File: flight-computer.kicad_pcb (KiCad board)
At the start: 2 copper layers, 50 x 62 mm, 49 parts, among them J1 Throttle/BEC, J2 Servo 1, J3 Servo 2, J4 Servo 3, J5 Servo 4, J6 Breakout1, J7 Power, J8 Ext, J9 Breakout2, SW1 SW_Push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

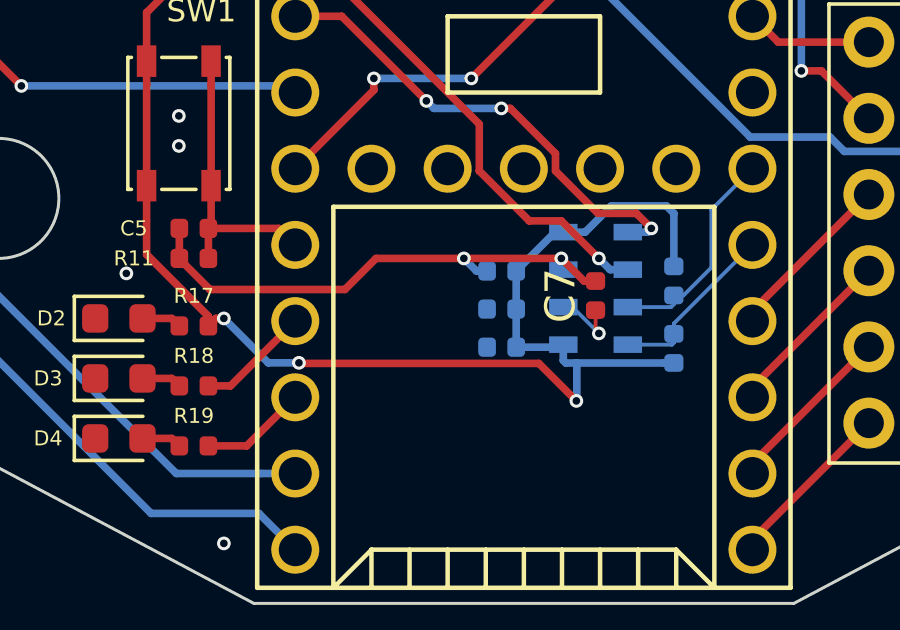
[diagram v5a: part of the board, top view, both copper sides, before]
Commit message: Fixed C4 footprint
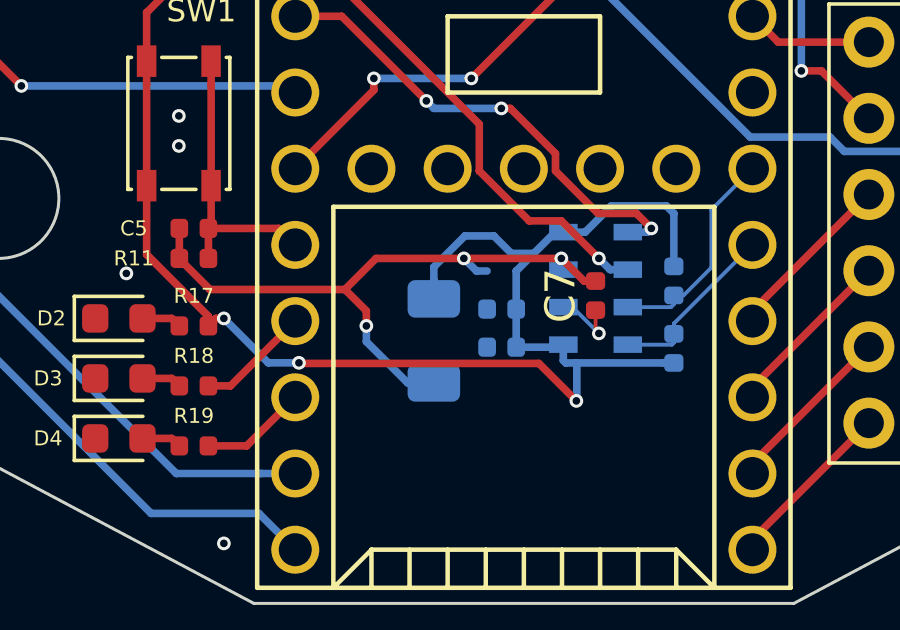
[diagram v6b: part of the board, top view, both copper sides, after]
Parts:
- C4: footprint Capacitor_SMD:C_0402_1005Metric -> Capacitor_SMD:C_1206_3216Metric
- moved C4 3.25 mm to (106.0, 103.2), turned to 270 degrees
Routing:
- net +3V3: track 133.9 -> 138.9 mm
- net GND: track 39.9 -> 44.8 mm, vias 22 -> 23
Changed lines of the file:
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@@
     (thickness 1.6)
     (drawings 12)
-    (tracks 431)
+    (tracks 444)
     (zones 0)
     (modules 49)
@@
     )
   )
-  (module Capacitor_SMD:C_0402_1005Metric (layer B.Cu)
-    (at 108.26 100.92 180)
-    (descr "Capacitor SMD 0402 (1005 Metric), square (rectangular) end terminal, IPC_7351 nominal, (Body size source: http://www.tortai-tech.com/upload/download/2011102023233369053.pdf), generated with kicad-footprint-generator")
-    (tags capacitor)
-    (attr smd)
-    (fp_text reference C4 (at 0 1.17) (layer B.SilkS)
-      (effects (font (size 1 1) (thickness 0.15)) (justify mirror))
-    )
-    (fp_text value 10uF (at 0 -1.17) (layer B.Fab)
-      (effects (font (size 1 1) (thickness 0.15)) (justify mirror))
-    )
-    (fp_text user %R (at 0 0) (layer B.Fab)
-      (effects (font (size 0.25 0.25) (thickness 0.04)) (justify mirror))
-    )
-    (fp_line (start 0.93 -0.47) (end -0.93 -0.47) (layer B.CrtYd) (width 0.05))
-    (fp_line (start 0.93 0.47) (end 0.93 -0.47) (layer B.CrtYd) (width 0.05))
-    (fp_line (start -0.93 0.47) (end 0.93 0.47) (layer B.CrtYd) (width 0.05))
-    (fp_line (start -0.93 -0.47) (end -0.93 0.47) (layer B.CrtYd) (width 0.05))
-    (fp_line (start 0.5 -0.25) (end -0.5 -0.25) (layer B.Fab) (width 0.1))
-    (fp_line (start 0.5 0.25) (end 0.5 -0.25) (layer B.Fab) (width 0.1))
-    (fp_line (start -0.5 0.25) (end 0.5 0.25) (layer B.Fab) (width 0.1))
-    (fp_line (start -0.5 -0.25) (end -0.5 0.25) (layer B.Fab) (width 0.1))
-    (pad 2 smd roundrect (at 0.485 0 180) (size 0.59 0.64) (layers B.Cu B.Paste B.Mask) (roundrect_rratio 0.25)
-      (net 2 GND))
-    (pad 1 smd roundrect (at -0.485 0 180) (size 0.59 0.64) (layers B.Cu B.Paste B.Mask) (roundrect_rratio 0.25)
-      (net 1 +3V3))
-    (model ${KISYS3DMOD}/Capacitor_SMD.3dshapes/C_0402_1005Metric.wrl
-      (at (xyz 0 0 0))
-      (scale (xyz 1 1 1))
-      (rotate (xyz 0 0 0))
-    )
-  )
   (module Capacitor_SMD:C_0402_1005Metric (layer F.Cu)
     (at 98 99.5 180)
@@
       (net 63 "Net-(D2-Pad2)"))
     (model ${KISYS3DMOD}/LED_SMD.3dshapes/LED_0603_1608Metric.wrl
+      (at (xyz 0 0 0))
+      (scale (xyz 1 1 1))
+      (rotate (xyz 0 0 0))
+    )
+  )
+  (module Capacitor_SMD:C_1206_3216Metric (layer B.Cu)
+    (at 106 103.25 270)
+    (descr "Capacitor SMD 1206 (3216 Metric), square (rectangular) end terminal, IPC_7351 nominal, (Body size source: http://www.tortai-tech.com/upload/download/2011102023233369053.pdf), generated with kicad-footprint-generator")
+    (tags capacitor)
+    (attr smd)
+    (fp_text reference C4 (at 0 1.82 90) (layer B.SilkS)
+      (effects (font (size 1 1) (thickness 0.15)) (justify mirror))
+    )
+    (fp_text value 10uF (at 0 -1.82 90) (layer B.Fab)
+      (effects (font (size 1 1) (thickness 0.15)) (justify mirror))
+    )
+    (fp_line (start -1.6 -0.8) (end -1.6 0.8) (layer B.Fab) (width 0.1))
+    (fp_line (start -1.6 0.8) (end 1.6 0.8) (layer B.Fab) (width 0.1))
+    (fp_line (start 1.6 0.8) (end 1.6 -0.8) (layer B.Fab) (width 0.1))
+    (fp_line (start 1.6 -0.8) (end -1.6 -0.8) (layer B.Fab) (width 0.1))
+    (fp_line (start -0.602064 0.91) (end 0.602064 0.91) (layer B.SilkS) (width 0.12))
+    (fp_line (start -0.602064 -0.91) (end 0.602064 -0.91) (layer B.SilkS) (width 0.12))
+    (fp_line (start -2.28 -1.12) (end -2.28 1.12) (layer B.CrtYd) (width 0.05))
+    (fp_line (start -2.28 1.12) (end 2.28 1.12) (layer B.CrtYd) (width 0.05))
+    (fp_line (start 2.28 1.12) (end 2.28 -1.12) (layer B.CrtYd) (width 0.05))
+    (fp_line (start 2.28 -1.12) (end -2.28 -1.12) (layer B.CrtYd) (width 0.05))
+    (fp_text user %R (at 0 0 90) (layer B.Fab)
+      (effects (font (size 0.8 0.8) (thickness 0.12)) (justify mirror))
+    )
+    (pad 1 smd roundrect (at -1.4 0 270) (size 1.25 1.75) (layers B.Cu B.Paste B.Mask) (roundrect_rratio 0.2)
+      (net 1 +3V3))
+    (pad 2 smd roundrect (at 1.4 0 270) (size 1.25 1.75) (layers B.Cu B.Paste B.Mask) (roundrect_rratio 0.2)
+      (net 2 GND))
+    (model ${KISYS3DMOD}/Capacitor_SMD.3dshapes/C_1206_3216Metric.wrl
       (at (xyz 0 0 0))
       (scale (xyz 1 1 1))
@@
   (segment (start 110.055 64.5) (end 109.58 64.025) (width 0.254) (layer B.Cu) (net 1))
   (segment (start 110.75 64.5) (end 110.055 64.5) (width 0.254) (layer B.Cu) (net 1))
-  (segment (start 110.04 99.625) (end 108.745 100.92) (width 0.254) (layer B.Cu) (net 1))
   (segment (start 110.315 99.625) (end 110.04 99.625) (width 0.254) (layer B.Cu) (net 1))
   (segment (start 108.745 100.92) (end 108.745 102.19) (width 0.254) (layer B.Cu) (net 1))
@@
   (segment (start 98.735 102.5) (end 98.485 102.75) (width 0.254) (layer F.Cu) (net 1))
   (segment (start 99 102.5) (end 98.735 102.5) (width 0.254) (layer F.Cu) (net 1))
+  (segment (start 109.3325 100.3325) (end 108.5825 100.3325) (width 0.254) (layer B.Cu) (net 1))
+  (segment (start 110.04 99.625) (end 109.3325 100.3325) (width 0.254) (layer B.Cu) (net 1))
+  (segment (start 109.3325 100.3325) (end 108.745 100.92) (width 0.254) (layer B.Cu) (net 1))
+  (segment (start 108.5825 100.3325) (end 108 99.75) (width 0.254) (layer B.Cu) (net 1))
+  (segment (start 106 101.225) (end 106 101.85) (width 0.254) (layer B.Cu) (net 1))
+  (segment (start 106 100.78575) (end 106 101.225) (width 0.254) (layer B.Cu) (net 1))
+  (segment (start 107.03575 99.75) (end 106 100.78575) (width 0.254) (layer B.Cu) (net 1))
+  (segment (start 108 99.75) (end 107.03575 99.75) (width 0.254) (layer B.Cu) (net 1))
   (via (at 129.25 62.75) (size 0.4572) (drill 0.254) (layers F.Cu B.Cu) (net 2))
   (via (at 127.25 60.5) (size 0.4572) (drill 0.254) (layers F.Cu B.Cu) (net 2))
@@
   (segment (start 106 76.5) (end 106.75 75.75) (width 0.254) (layer F.Cu) (net 2))
   (segment (start 106 80) (end 106 76.5) (width 0.254) (layer F.Cu) (net 2))
+  (via (at 103.75 102.75) (size 0.4572) (drill 0.254) (layers F.Cu B.Cu) (net 2))
+  (segment (start 105.125 104.65) (end 103.75 103.275) (width 0.254) (layer B.Cu) (net 2))
+  (segment (start 103.75 103.275) (end 103.75 102.75) (width 0.254) (layer B.Cu) (net 2))
+  (segment (start 106 104.65) (end 105.125 104.65) (width 0.254) (layer B.Cu) (net 2))
+  (segment (start 103.75 102.25) (end 103.035999 101.535999) (width 0.254) (layer F.Cu) (net 2))
+  (segment (start 103.75 102.75) (end 103.75 102.25) (width 0.254) (layer F.Cu) (net 2))
   (segment (start 98.575 99.41) (end 98.485 99.5) (width 0.254) (layer F.Cu) (net 3))
   (segment (start 98.575 98.075) (end 98.575 99.41) (width 0.254) (layer F.Cu) (net 3))

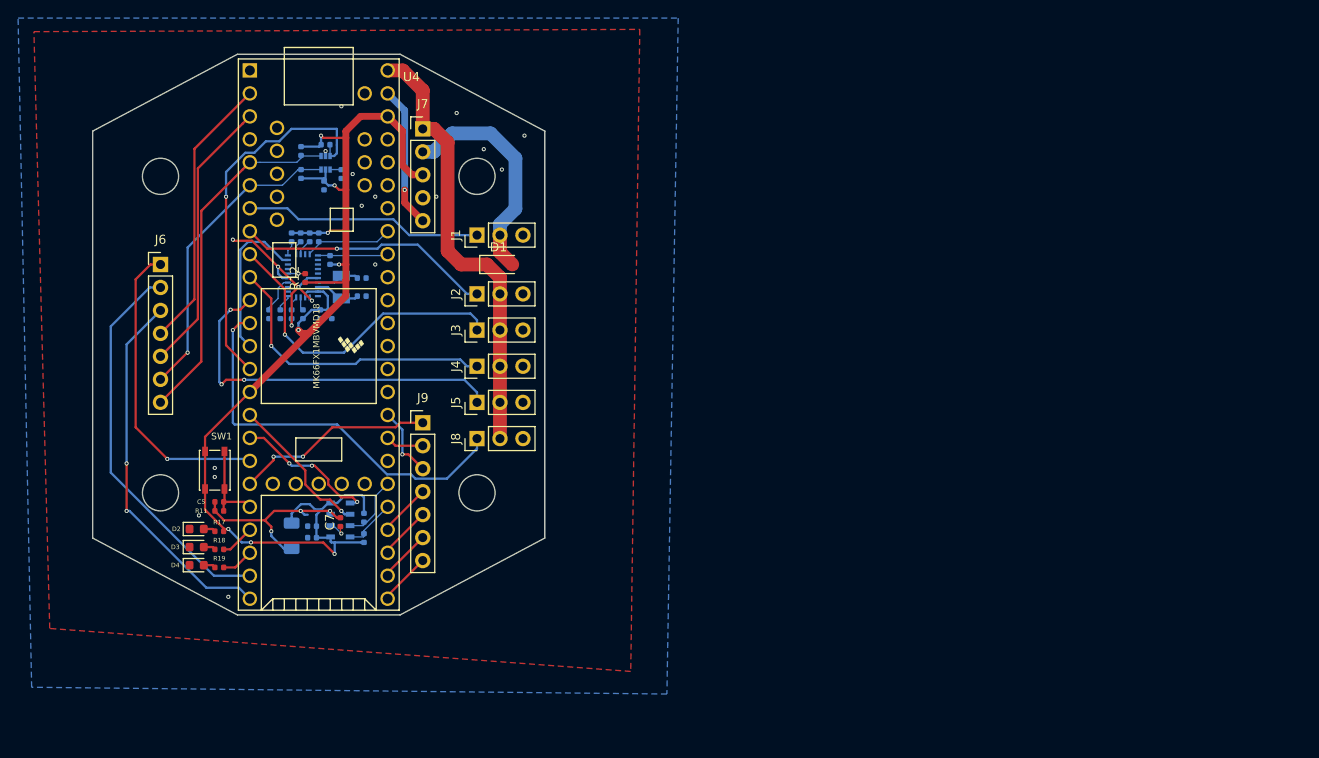
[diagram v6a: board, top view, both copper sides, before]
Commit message: Revamped routing
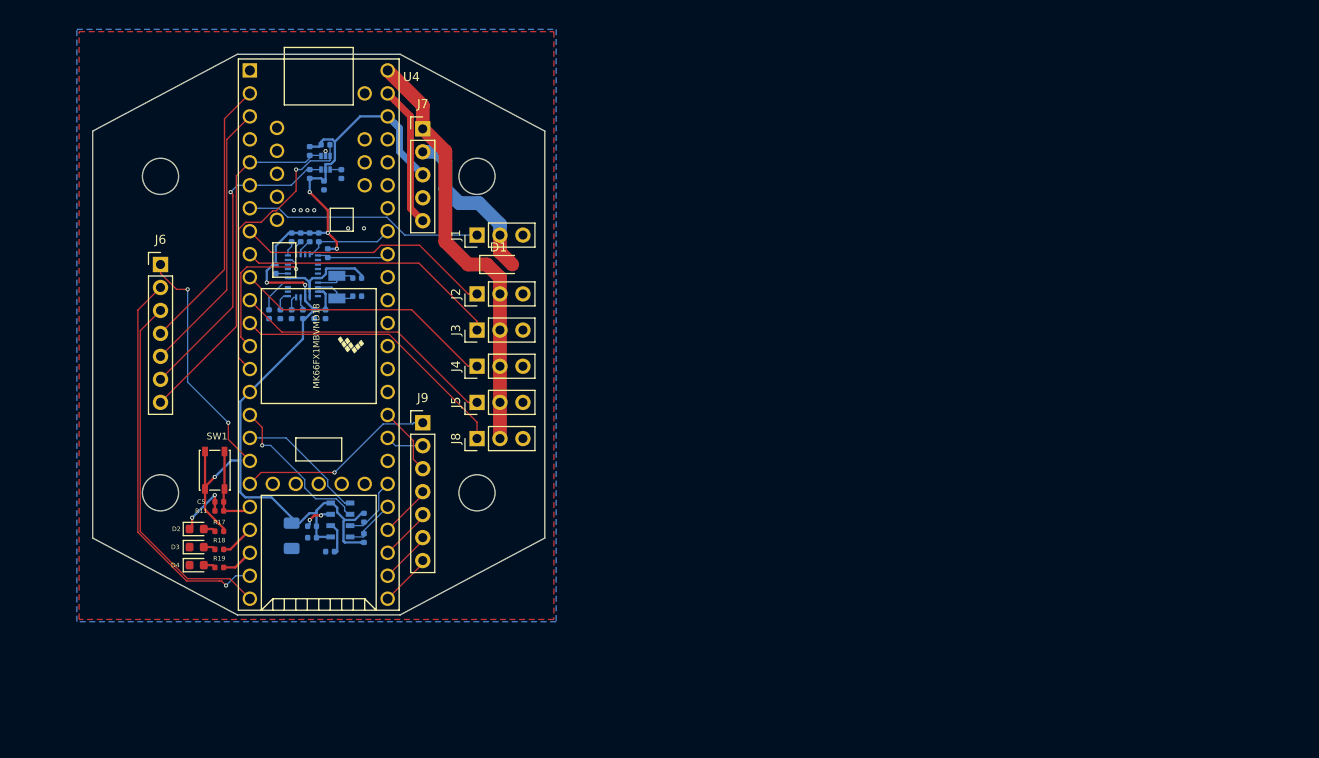
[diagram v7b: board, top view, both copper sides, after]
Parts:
- C7, R12: moved to B.Cu
- moved C7 3.45 mm to (110.2, 105.0), turned to 180 degrees
- moved R12 3.40 mm to (104.2, 73.8), turned to 270 degrees
- moved R3 0.96 mm to (108.0, 63.2)
- moved R4 0.96 mm to (108.0, 60.7)
- moved R5 0.79 mm to (110.0, 72.0), turned to 270 degrees
- moved C3 0.69 mm to (109.8, 78.8)
- moved C2 0.67 mm to (108.5, 78.8)
- moved C10 0.50 mm to (113.2, 76.8)
- moved C11 0.50 mm to (113.2, 74.8)
- moved Y1 0.50 mm to (111.0, 75.8)
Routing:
- net GND: track 44.8 -> 23.2 mm, vias 23 -> 11
- net +3V3: track 138.9 -> 123.6 mm, vias 8 -> 6
- net /EXT: track 44.5 -> 31.5 mm, vias 1 -> 0
- net /SER4: track 41.6 -> 29.8 mm, vias 3 -> 0
- net /TMP_INT: track 41.9 -> 32.4 mm
- net /D26: track 34.0 -> 26.5 mm, vias 1 -> 2
- net /SER2: track 35.8 -> 29.2 mm, vias 1 -> 0
- net /VBEC: track 25.3 -> 18.7 mm
- net /SER3: track 32.7 -> 29.2 mm, vias 1 -> 0
- net /VIN: track 49.2 -> 47.1 mm
- net /ALT_INT_2: track 16.0 -> 14.5 mm, vias 3 -> 0
- net Net-(C7-Pad1): track 2.37 -> 3.59 mm, vias 1 -> 0
- net /ALT_INT_1: track 16.5 -> 17.6 mm
- net /SDA2: track 34.2 -> 35.2 mm
- net /IMU_INT: track 17.5 -> 16.6 mm, vias 0 -> 1
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
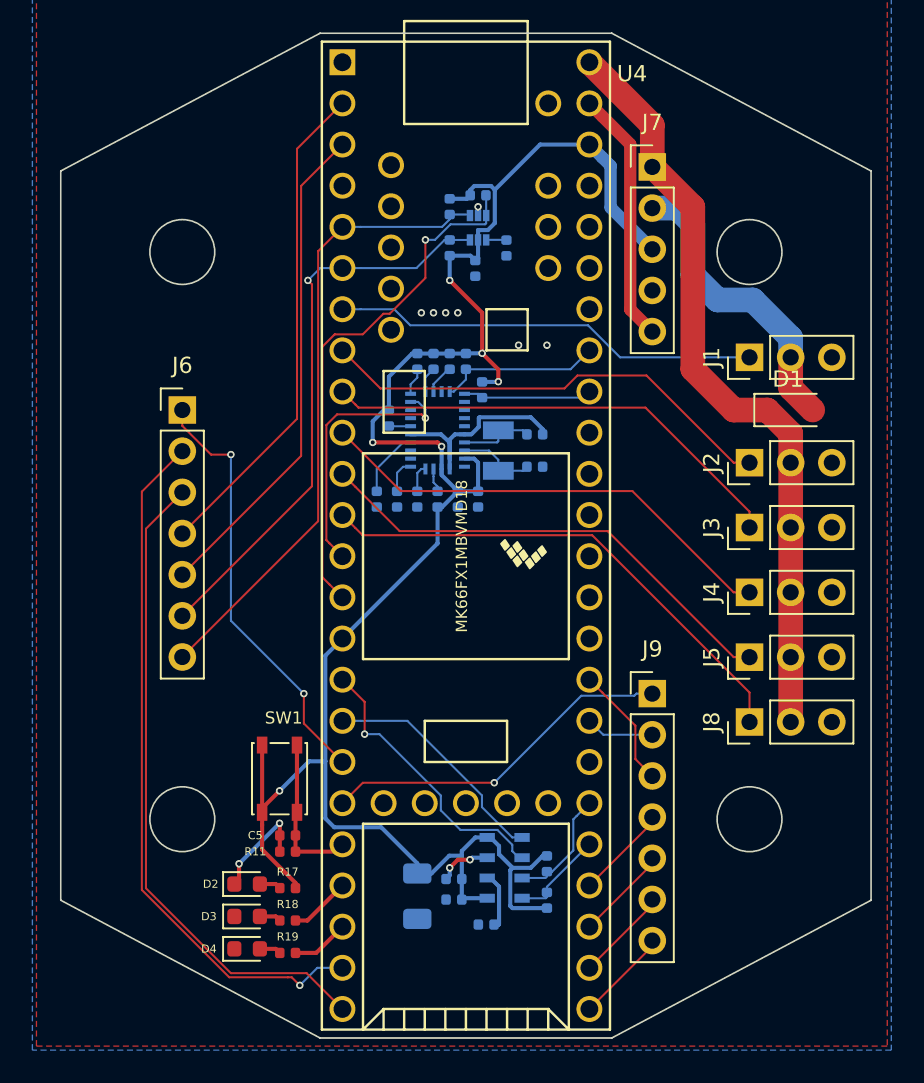
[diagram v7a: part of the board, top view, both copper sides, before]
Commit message: Added mounting hole pads
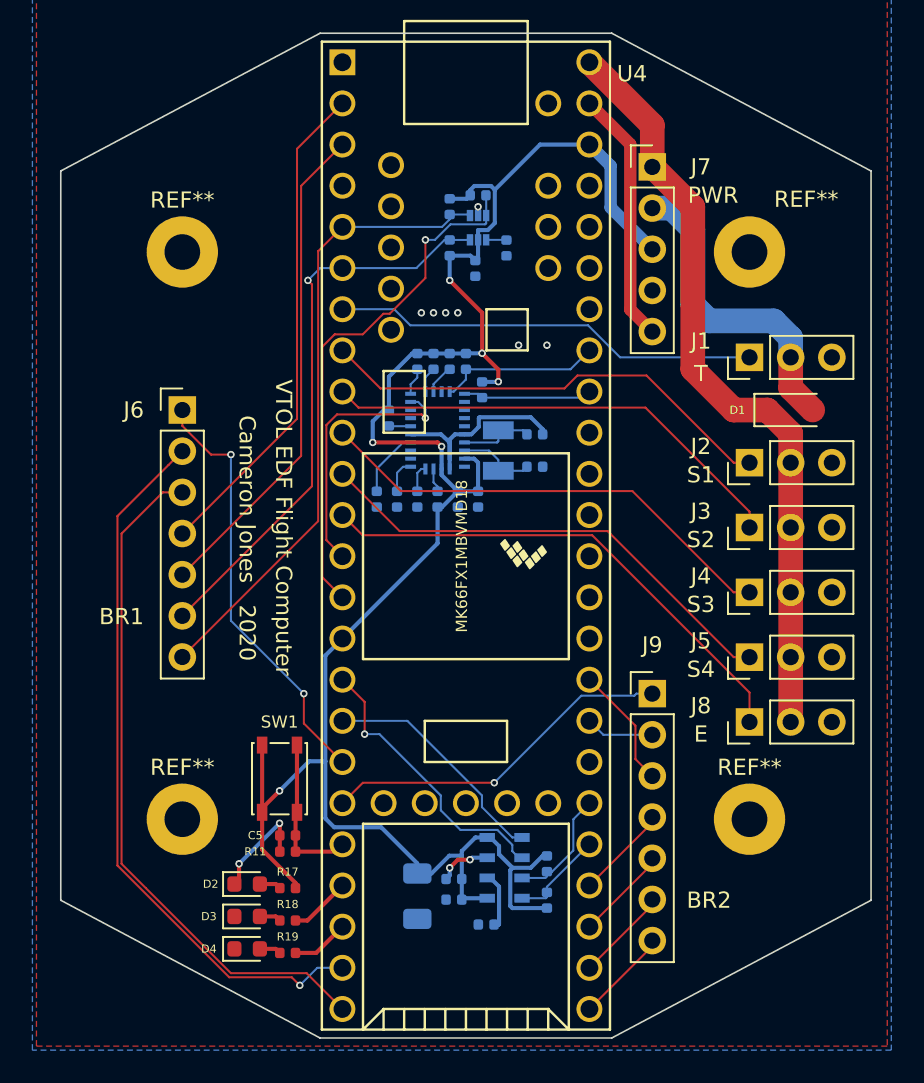
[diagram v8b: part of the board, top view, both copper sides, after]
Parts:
- added REF**: MountingHole_2.2mm_M2_Pad, MountingHole:MountingHole_2.2mm_M2_Pad, F.Cu at (126.5, 63.5)
- added REF**: MountingHole_2.2mm_M2_Pad, MountingHole:MountingHole_2.2mm_M2_Pad, F.Cu at (91.5, 63.5)
- added REF**: MountingHole_2.2mm_M2_Pad, MountingHole:MountingHole_2.2mm_M2_Pad, F.Cu at (91.5, 98.5)
- added REF**: MountingHole_2.2mm_M2_Pad, MountingHole:MountingHole_2.2mm_M2_Pad, F.Cu at (126.5, 98.5)
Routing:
- net /D32: track 40.6 -> 42.5 mm
- net /D31: track 43.4 -> 44.6 mm
- net /VBEC: track 18.7 -> 19.6 mm
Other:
- outline, holes or cut-outs redrawn
- board text added: "2020"
- board text added: "BR1"
- board text added: "BR2"
- board text added: "Cameron Jones"
- board text added: "E"
- board text added: "PWR"
- board text added: "S1"
- board text added: "S2"
- board text added: "S3"
- board text added: "S4"
- board text added: "T"
- board text added: "VTOL EDF Flight Computer"
